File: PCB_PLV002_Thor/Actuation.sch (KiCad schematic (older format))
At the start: 59 parts

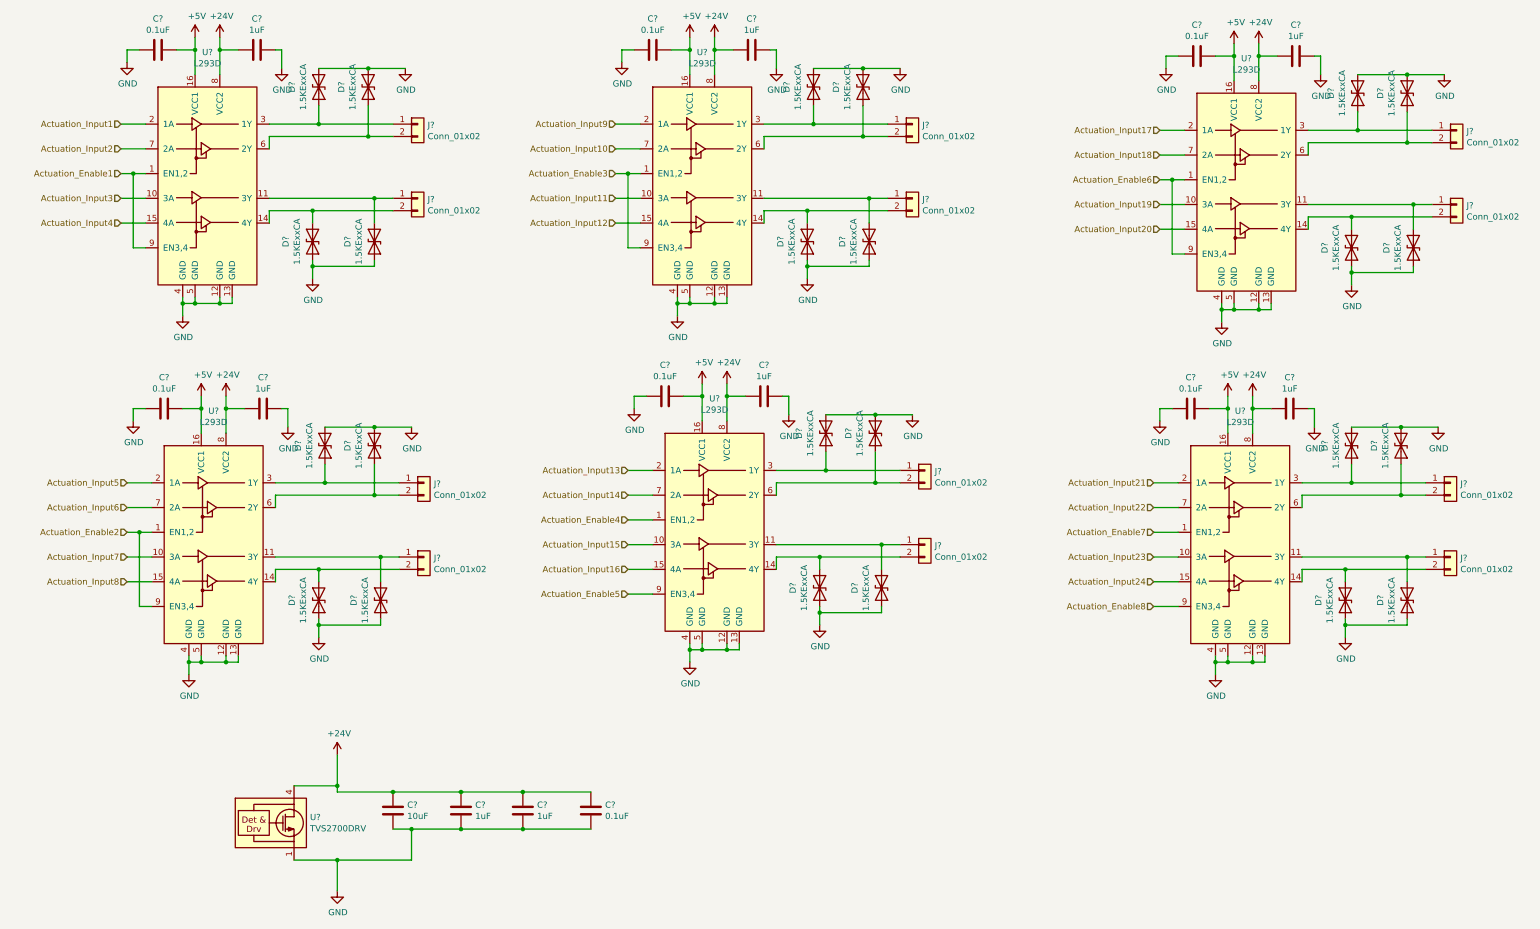
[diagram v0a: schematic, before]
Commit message: Finish schematic
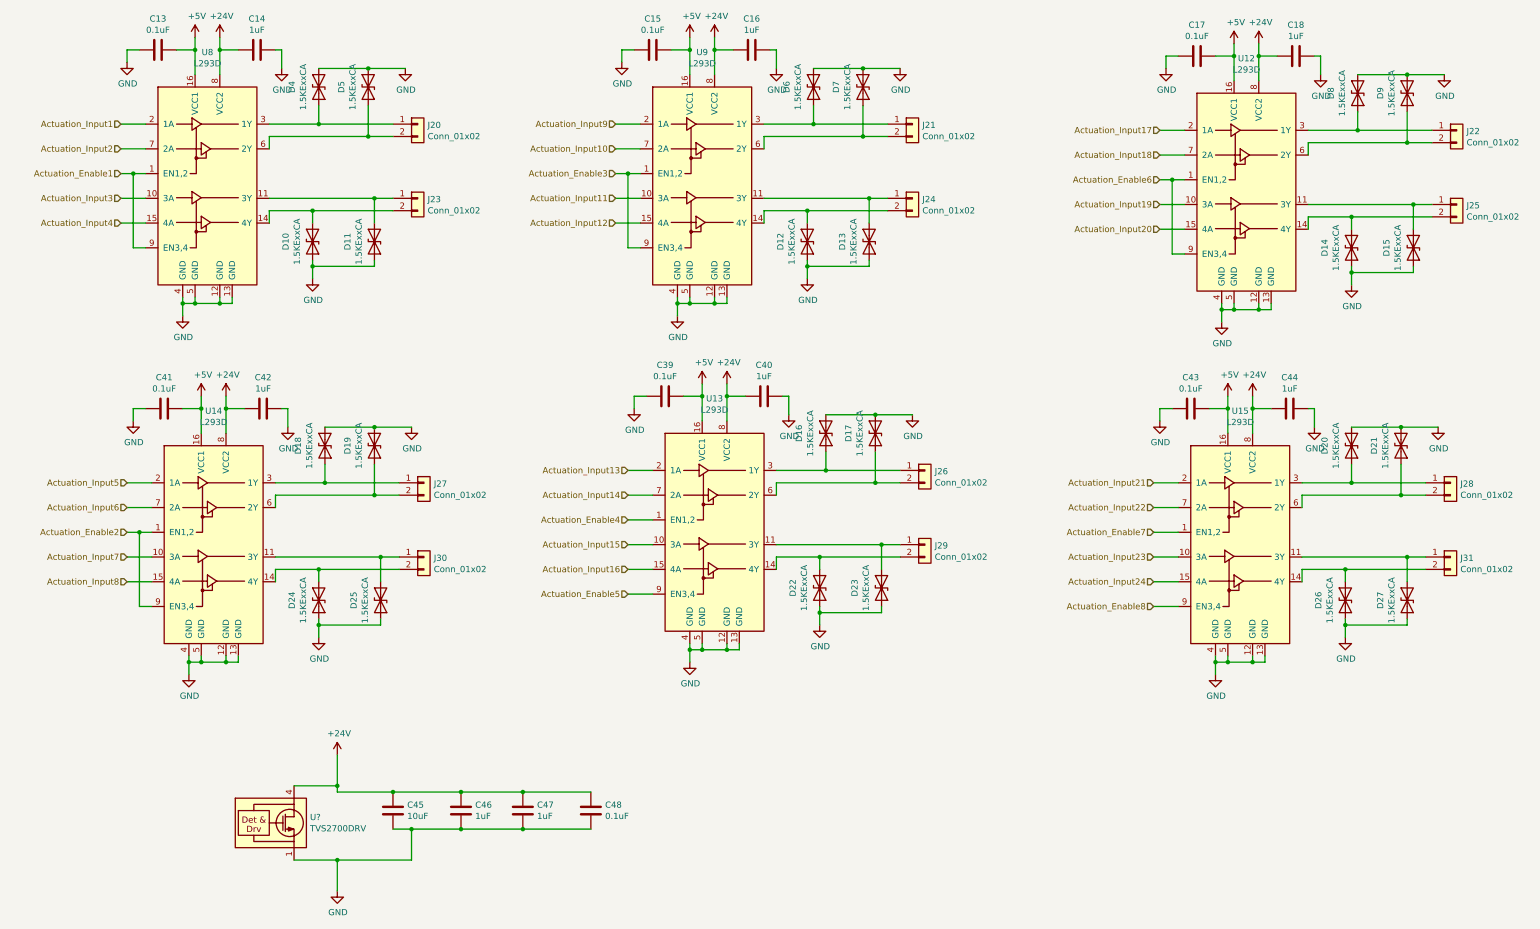
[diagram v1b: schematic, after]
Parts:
- gave numbers to parts that had none: 58
